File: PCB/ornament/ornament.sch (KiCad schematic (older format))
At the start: 40 parts, among them J1 USB_B_Micro, J3 Conn_01x06, SW1 MODE, U1 PIC16F18325-ISL

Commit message: printouts
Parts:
- J1: Note (none) -> 28-00111-U
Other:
- note removed: "28-00111-U"
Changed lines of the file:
@@
 	1300 3800 1350 3800
 Connection ~ 1350 3800
-Text Notes 1650 3750 0    50   ~ 0
-28-00111-U
 $Comp
 L Connector:USB_B_Micro J1
@@
 F 2 "Connector_USB:USB_Micro-B_Molex-105017-0001" H 1550 3250 50  0001 C CNN
 F 3 "~" H 1550 3250 50  0001 C CNN
+F 4 "28-00111-U" H 1400 3300 50  0001 C CNN "Note"
 	1    1400 3300
 	1    0    0    -1

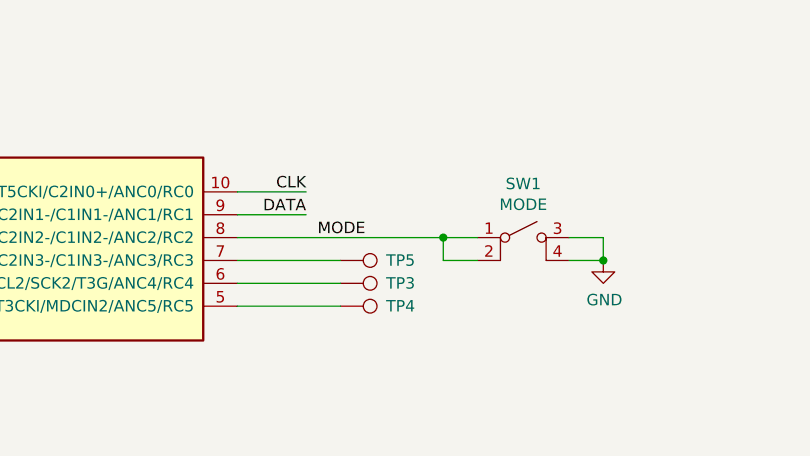
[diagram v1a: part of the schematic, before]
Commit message: routed PCB, about to upgrade kicad
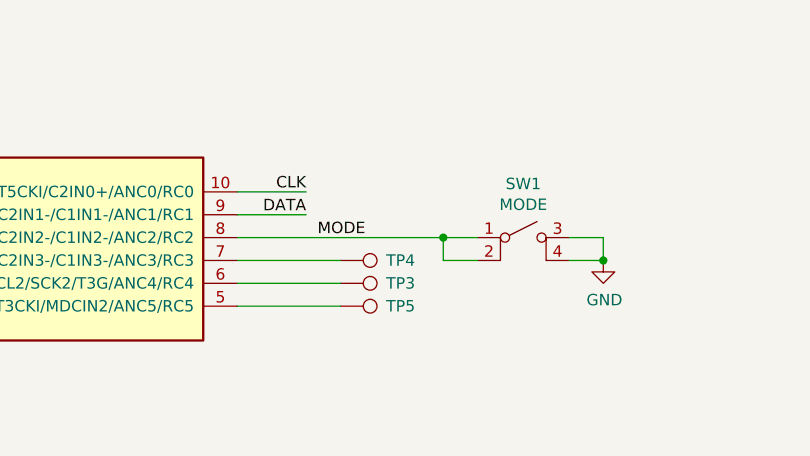
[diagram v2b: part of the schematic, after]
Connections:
- net at U1.5 (DT/RX/SDA2/SDI2/CCP1/T3CKI/MDCIN2/ANC5/RC5): now also TP5.1; no longer TP4.1
- net at U1.7 (CLCIN0/~SS1~/CCP2/T5G/MDMIN/C2IN3-/C1IN3-/ANC3/RC3): now also TP4.1; no longer TP5.1
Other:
- moved on the sheet: TP4, TP5
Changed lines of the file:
@@
 	1500 5000 1100 5000
-Wire Wire Line
-	2200 4900 1650 4900
 Wire Wire Line
 	1650 4900 1650 5100
@@
 L Connector:TestPoint TP5
 U 1 1 6323B982
-P 7650 5200
-F 0 "TP5" V 7650 5400 50  0000 L CNN
-F 1 "TP5" V 7650 5700 50  0001 L CNN
-F 2 "TestPoint:TestPoint_Plated_Hole_D2.0mm" H 7850 5200 50  0001 C CNN
-F 3 "~" H 7850 5200 50  0001 C CNN
-	1    7650 5200
+P 7650 5400
+F 0 "TP5" V 7650 5600 50  0000 L CNN
+F 1 "TP5" V 7650 5900 50  0001 L CNN
+F 2 "TestPoint:TestPoint_Plated_Hole_D2.0mm" H 7850 5400 50  0001 C CNN
+F 3 "~" H 7850 5400 50  0001 C CNN
+	1    7650 5400
 	0    1    1    0
 $EndComp
@@
 L Connector:TestPoint TP4
 U 1 1 6323BC84
-P 7650 5400
-F 0 "TP4" V 7650 5600 50  0000 L CNN
-F 1 "TP4" V 7650 5900 50  0001 L CNN
-F 2 "TestPoint:TestPoint_Plated_Hole_D2.0mm" H 7850 5400 50  0001 C CNN
-F 3 "~" H 7850 5400 50  0001 C CNN
-	1    7650 5400
+P 7650 5200
+F 0 "TP4" V 7650 5400 50  0000 L CNN
+F 1 "TP4" V 7650 5700 50  0001 L CNN
+F 2 "TestPoint:TestPoint_Plated_Hole_D2.0mm" H 7850 5200 50  0001 C CNN
+F 3 "~" H 7850 5200 50  0001 C CNN
+	1    7650 5200
 	0    1    1    0
 $EndComp
@@
 	8650 5200 8800 5200
 Connection ~ 8800 5200
+Wire Wire Line
+	2200 4900 1650 4900
 $EndSCHEMATC
